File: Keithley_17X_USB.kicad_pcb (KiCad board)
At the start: 2 copper layers, 91.5 x 44 mm, 42 parts, among them J1 USB_B, J2 SIGNAL INPUT, J3 PROG, U1 TLP281-4, U2 TLP281-4, U3 MIC5504-3.3YM5, U4 MSP430FR2110, U5 FT230XS

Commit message: rearaned B1 B2 B4 and B8 connection to opto for better layout
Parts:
- moved U4 71.8 mm to (95.8, 56.2), turned to 90 degrees
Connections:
- J2 pad 3: /B8_IN -> /B1_IN
- J2 pad 5: /B4_IN -> /B2_IN
- J2 pad 7: /B2_IN -> /B4_IN
- J2 pad 9: /B1_IN -> /B8_IN
- U2 pad 1: /B1_IN -> /B8_IN
- U2 pad 10: /B8 -> /B1
- U2 pad 12: /B4 -> /B2
- U2 pad 14: /B2 -> /B4
- U2 pad 16: /B1 -> /B8
- U2 pad 3: /B2_IN -> /B4_IN
- U2 pad 5: /B4_IN -> /B2_IN
- U2 pad 7: /B8_IN -> /B1_IN
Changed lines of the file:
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@@
     (pad 2 thru_hole oval (at 2.54 0 180) (size 1.7 1.7) (drill 1) (layers *.Cu *.Mask))
     (pad 3 thru_hole oval (at 0 -2.54 180) (size 1.7 1.7) (drill 1) (layers *.Cu *.Mask)
-      (net 19 /B8_IN))
+      (net 23 /B1_IN))
     (pad 4 thru_hole oval (at 2.54 -2.54 180) (size 1.7 1.7) (drill 1) (layers *.Cu *.Mask))
     (pad 5 thru_hole oval (at 0 -5.08 180) (size 1.7 1.7) (drill 1) (layers *.Cu *.Mask)
-      (net 20 /B4_IN))
+      (net 22 /B2_IN))
     (pad 6 thru_hole oval (at 2.54 -5.08 180) (size 1.7 1.7) (drill 1) (layers *.Cu *.Mask)
       (net 21 /SIGN_IN))
     (pad 7 thru_hole oval (at 0 -7.62 180) (size 1.7 1.7) (drill 1) (layers *.Cu *.Mask)
-      (net 22 /B2_IN))
+      (net 20 /B4_IN))
     (pad 8 thru_hole oval (at 2.54 -7.62 180) (size 1.7 1.7) (drill 1) (layers *.Cu *.Mask))
     (pad 9 thru_hole oval (at 0 -10.16 180) (size 1.7 1.7) (drill 1) (layers *.Cu *.Mask)
-      (net 23 /B1_IN))
+      (net 19 /B8_IN))
     (pad 10 thru_hole oval (at 2.54 -10.16 180) (size 1.7 1.7) (drill 1) (layers *.Cu *.Mask))
     (pad 11 thru_hole oval (at 0 -12.7 180) (size 1.7 1.7) (drill 1) (layers *.Cu *.Mask)
@@
     (fp_line (start 0 5.26) (end 2.275 5.26) (layer F.SilkS) (width 0.12))
     (pad 16 smd roundrect (at 3.25 -4.445) (size 1.6 0.55) (layers F.Cu F.Paste F.Mask) (roundrect_rratio 0.25)
+      (net 49 /B8))
+    (pad 15 smd roundrect (at 3.25 -3.175) (size 1.6 0.55) (layers F.Cu F.Paste F.Mask) (roundrect_rratio 0.25)
+      (net 2 GND))
+    (pad 14 smd roundrect (at 3.25 -1.905) (size 1.6 0.55) (layers F.Cu F.Paste F.Mask) (roundrect_rratio 0.25)
+      (net 48 /B4))
+    (pad 13 smd roundrect (at 3.25 -0.635) (size 1.6 0.55) (layers F.Cu F.Paste F.Mask) (roundrect_rratio 0.25)
+      (net 2 GND))
+    (pad 12 smd roundrect (at 3.25 0.635) (size 1.6 0.55) (layers F.Cu F.Paste F.Mask) (roundrect_rratio 0.25)
+      (net 47 /B2))
+    (pad 11 smd roundrect (at 3.25 1.905) (size 1.6 0.55) (layers F.Cu F.Paste F.Mask) (roundrect_rratio 0.25)
+      (net 2 GND))
+    (pad 10 smd roundrect (at 3.25 3.175) (size 1.6 0.55) (layers F.Cu F.Paste F.Mask) (roundrect_rratio 0.25)
       (net 46 /B1))
-    (pad 15 smd roundrect (at 3.25 -3.175) (size 1.6 0.55) (layers F.Cu F.Paste F.Mask) (roundrect_rratio 0.25)
-      (net 2 GND))
-    (pad 14 smd roundrect (at 3.25 -1.905) (size 1.6 0.55) (layers F.Cu F.Paste F.Mask) (roundrect_rratio 0.25)
-      (net 47 /B2))
-    (pad 13 smd roundrect (at 3.25 -0.635) (size 1.6 0.55) (layers F.Cu F.Paste F.Mask) (roundrect_rratio 0.25)
-      (net 2 GND))
-    (pad 12 smd roundrect (at 3.25 0.635) (size 1.6 0.55) (layers F.Cu F.Paste F.Mask) (roundrect_rratio 0.25)
-      (net 48 /B4))
-    (pad 11 smd roundrect (at 3.25 1.905) (size 1.6 0.55) (layers F.Cu F.Paste F.Mask) (roundrect_rratio 0.25)
-      (net 2 GND))
-    (pad 10 smd roundrect (at 3.25 3.175) (size 1.6 0.55) (layers F.Cu F.Paste F.Mask) (roundrect_rratio 0.25)
-      (net 49 /B8))
     (pad 9 smd roundrect (at 3.25 4.445) (size 1.6 0.55) (layers F.Cu F.Paste F.Mask) (roundrect_rratio 0.25)
       (net 2 GND))
@@
       (net 41 "Net-(RN2-Pad5)"))
     (pad 7 smd roundrect (at -3.25 3.175) (size 1.6 0.55) (layers F.Cu F.Paste F.Mask) (roundrect_rratio 0.25)
-      (net 19 /B8_IN))
+      (net 23 /B1_IN))
     (pad 6 smd roundrect (at -3.25 1.905) (size 1.6 0.55) (layers F.Cu F.Paste F.Mask) (roundrect_rratio 0.25)
       (net 40 "Net-(RN2-Pad6)"))
     (pad 5 smd roundrect (at -3.25 0.635) (size 1.6 0.55) (layers F.Cu F.Paste F.Mask) (roundrect_rratio 0.25)
-      (net 20 /B4_IN))
+      (net 22 /B2_IN))
     (pad 4 smd roundrect (at -3.25 -0.635) (size 1.6 0.55) (layers F.Cu F.Paste F.Mask) (roundrect_rratio 0.25)
       (net 39 "Net-(RN2-Pad7)"))
     (pad 3 smd roundrect (at -3.25 -1.905) (size 1.6 0.55) (layers F.Cu F.Paste F.Mask) (roundrect_rratio 0.25)
-      (net 22 /B2_IN))
+      (net 20 /B4_IN))
     (pad 2 smd roundrect (at -3.25 -3.175) (size 1.6 0.55) (layers F.Cu F.Paste F.Mask) (roundrect_rratio 0.25)
       (net 38 "Net-(RN2-Pad8)"))
     (pad 1 smd roundrect (at -3.25 -4.445) (size 1.6 0.55) (layers F.Cu F.Paste F.Mask) (roundrect_rratio 0.25)
-      (net 23 /B1_IN))
+      (net 19 /B8_IN))
     (model ${KIPRJMOD}/3d_models/SOIC-16_3.9x9.9mm_p1.27mm.wrl
       (at (xyz 0 0 0))
@@
   )
   (module Package_SO:TSSOP-16_4.4x5mm_P0.65mm (layer F.Cu)
-    (at 46 108)
+    (at 95.75 56.25 90)
     (descr "16-Lead Plastic Thin Shrink Small Outline (ST)-4.4 mm Body [TSSOP] (see Microchip Packaging Specification 00000049BS.pdf)")
     (tags "SSOP 0.65")
     (attr smd)
-    (fp_text reference U4 (at 0 -3.55) (layer F.SilkS)
-      (effects (font (size 1 1) (thickness 0.15)))
-    )
-    (fp_text value MSP430FR2110 (at 0 3.55) (layer F.Fab)
+    (fp_text reference U4 (at 0 -3.55 90) (layer F.SilkS)
+      (effects (font (size 1 1) (thickness 0.15)))
+    )
+    (fp_text value MSP430FR2110 (at 0 3.55 90) (layer F.Fab)
       (effects (font (size 1 1) (thickness 0.15)))
     )
@@
     (fp_line (start -2.2 2.725) (end 2.2 2.725) (layer F.SilkS) (width 0.15))
     (fp_line (start -3.775 -2.8) (end 2.2 -2.8) (layer F.SilkS) (width 0.15))
-    (fp_text user %R (at 0 0) (layer F.Fab)
+    (fp_text user %R (at 0 0 90) (layer F.Fab)
       (effects (font (size 0.8 0.8) (thickness 0.15)))
     )
-    (pad 1 smd rect (at -2.95 -2.275) (size 1.5 0.45) (layers F.Cu F.Paste F.Mask)
+    (pad 1 smd rect (at -2.95 -2.275 90) (size 1.5 0.45) (layers F.Cu F.Paste F.Mask)
       (net 47 /B2))
-    (pad 2 smd rect (at -2.95 -1.625) (size 1.5 0.45) (layers F.Cu F.Paste F.Mask)
+    (pad 2 smd rect (at -2.95 -1.625 90) (size 1.5 0.45) (layers F.Cu F.Paste F.Mask)
       (net 46 /B1))
-    (pad 3 smd rect (at -2.95 -0.975) (size 1.5 0.45) (layers F.Cu F.Paste F.Mask)
+    (pad 3 smd rect (at -2.95 -0.975 90) (size 1.5 0.45) (layers F.Cu F.Paste F.Mask)
       (net 28 /SBWTCK))
-    (pad 4 smd rect (at -2.95 -0.325) (size 1.5 0.45) (layers F.Cu F.Paste F.Mask)
+    (pad 4 smd rect (at -2.95 -0.325 90) (size 1.5 0.45) (layers F.Cu F.Paste F.Mask)
       (net 27 /SBWTDIO))
-    (pad 5 smd rect (at -2.95 0.325) (size 1.5 0.45) (layers F.Cu F.Paste F.Mask)
+    (pad 5 smd rect (at -2.95 0.325 90) (size 1.5 0.45) (layers F.Cu F.Paste F.Mask)
       (net 3 +3V3))
-    (pad 6 smd rect (at -2.95 0.975) (size 1.5 0.45) (layers F.Cu F.Paste F.Mask)
-      (net 2 GND))
-    (pad 7 smd rect (at -2.95 1.625) (size 1.5 0.45) (layers F.Cu F.Paste F.Mask)
+    (pad 6 smd rect (at -2.95 0.975 90) (size 1.5 0.45) (layers F.Cu F.Paste F.Mask)
+      (net 2 GND))
+    (pad 7 smd rect (at -2.95 1.625 90) (size 1.5 0.45) (layers F.Cu F.Paste F.Mask)
       (net 42 /OVERRANGE))
-    (pad 8 smd rect (at -2.95 2.275) (size 1.5 0.45) (layers F.Cu F.Paste F.Mask)
+    (pad 8 smd rect (at -2.95 2.275 90) (size 1.5 0.45) (layers F.Cu F.Paste F.Mask)
       (net 43 /SIGN))
-    (pad 9 smd rect (at 2.95 2.275) (size 1.5 0.45) (layers F.Cu F.Paste F.Mask)
+    (pad 9 smd rect (at 2.95 2.275 90) (size 1.5 0.45) (layers F.Cu F.Paste F.Mask)
       (net 44 /D5))
-    (pad 10 smd rect (at 2.95 1.625) (size 1.5 0.45) (layers F.Cu F.Paste F.Mask)
+    (pad 10 smd rect (at 2.95 1.625 90) (size 1.5 0.45) (layers F.Cu F.Paste F.Mask)
       (net 45 /CLK))
-    (pad 11 smd rect (at 2.95 0.975) (size 1.5 0.45) (layers F.Cu F.Paste F.Mask)
+    (pad 11 smd rect (at 2.95 0.975 90) (size 1.5 0.45) (layers F.Cu F.Paste F.Mask)
       (net 50 /RXD))
-    (pad 12 smd rect (at 2.95 0.325) (size 1.5 0.45) (layers F.Cu F.Paste F.Mask)
+    (pad 12 smd rect (at 2.95 0.325 90) (size 1.5 0.45) (layers F.Cu F.Paste F.Mask)
       (net 51 /TXD))
-    (pad 13 smd rect (at 2.95 -0.325) (size 1.5 0.45) (layers F.Cu F.Paste F.Mask)
+    (pad 13 smd rect (at 2.95 -0.325 90) (size 1.5 0.45) (layers F.Cu F.Paste F.Mask)
       (net 30 /RATE))
-    (pad 14 smd rect (at 2.95 -0.975) (size 1.5 0.45) (layers F.Cu F.Paste F.Mask)
+    (pad 14 smd rect (at 2.95 -0.975 90) (size 1.5 0.45) (layers F.Cu F.Paste F.Mask)
       (net 16 /READ))
-    (pad 15 smd rect (at 2.95 -1.625) (size 1.5 0.45) (layers F.Cu F.Paste F.Mask)
+    (pad 15 smd rect (at 2.95 -1.625 90) (size 1.5 0.45) (layers F.Cu F.Paste F.Mask)
       (net 49 /B8))
-    (pad 16 smd rect (at 2.95 -2.275) (size 1.5 0.45) (layers F.Cu F.Paste F.Mask)
+    (pad 16 smd rect (at 2.95 -2.275 90) (size 1.5 0.45) (layers F.Cu F.Paste F.Mask)
       (net 48 /B4))
     (model ${KISYS3DMOD}/Package_SO.3dshapes/TSSOP-16_4.4x5mm_P0.65mm.wrl

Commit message: update 3d model to shrouded header
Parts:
- moved U5 16.5 mm to (116.5, 67.0)
- moved U2 9.72 mm to (73.0, 63.8)
- moved U1 6.32 mm to (73.0, 79.0)
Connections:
- J2 pad 3: /B1_IN -> /B8_IN
- J2 pad 5: /B2_IN -> /B4_IN
- J2 pad 7: /B4_IN -> /B2_IN
- J2 pad 9: /B8_IN -> /B1_IN
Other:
- board size 91.5 x 44 mm -> 87 x 44 mm
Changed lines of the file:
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@@
     (pad 2 thru_hole oval (at 2.54 0 180) (size 1.7 1.7) (drill 1) (layers *.Cu *.Mask))
     (pad 3 thru_hole oval (at 0 -2.54 180) (size 1.7 1.7) (drill 1) (layers *.Cu *.Mask)
-      (net 23 /B1_IN))
+      (net 19 /B8_IN))
     (pad 4 thru_hole oval (at 2.54 -2.54 180) (size 1.7 1.7) (drill 1) (layers *.Cu *.Mask))
     (pad 5 thru_hole oval (at 0 -5.08 180) (size 1.7 1.7) (drill 1) (layers *.Cu *.Mask)
-      (net 22 /B2_IN))
+      (net 20 /B4_IN))
     (pad 6 thru_hole oval (at 2.54 -5.08 180) (size 1.7 1.7) (drill 1) (layers *.Cu *.Mask)
       (net 21 /SIGN_IN))
     (pad 7 thru_hole oval (at 0 -7.62 180) (size 1.7 1.7) (drill 1) (layers *.Cu *.Mask)
-      (net 20 /B4_IN))
+      (net 22 /B2_IN))
     (pad 8 thru_hole oval (at 2.54 -7.62 180) (size 1.7 1.7) (drill 1) (layers *.Cu *.Mask))
     (pad 9 thru_hole oval (at 0 -10.16 180) (size 1.7 1.7) (drill 1) (layers *.Cu *.Mask)
-      (net 19 /B8_IN))
+      (net 23 /B1_IN))
     (pad 10 thru_hole oval (at 2.54 -10.16 180) (size 1.7 1.7) (drill 1) (layers *.Cu *.Mask))
     (pad 11 thru_hole oval (at 0 -12.7 180) (size 1.7 1.7) (drill 1) (layers *.Cu *.Mask)
@@
       (net 26 /D5_IN))
     (pad 14 thru_hole oval (at 2.54 -15.24 180) (size 1.7 1.7) (drill 1) (layers *.Cu *.Mask))
-    (model ${KISYS3DMOD}/Connector_PinHeader_2.54mm.3dshapes/PinHeader_2x07_P2.54mm_Horizontal.wrl
+    (model ${KIPRJMOD}/3d_models/Header_14pos_2rows_RightAngle_Shrouded.wrl
       (at (xyz 0 0 0))
       (scale (xyz 1 1 1))
@@
   )
   (module Package_SO:SOIC-16_4.55x10.3mm_P1.27mm (layer F.Cu)
-    (at 79 77)
+    (at 73 79)
     (descr "SOIC, 16 Pin (https://toshiba.semicon-storage.com/info/docget.jsp?did=12858&prodName=TLP291-4), generated with kicad-footprint-generator ipc_gullwing_generator.py")
     (tags "SOIC SO")
@@
   )
   (module Package_SO:SOIC-16_4.55x10.3mm_P1.27mm (layer F.Cu)
-    (at 80 57)
+    (at 73 63.75)
     (descr "SOIC, 16 Pin (https://toshiba.semicon-storage.com/info/docget.jsp?did=12858&prodName=TLP291-4), generated with kicad-footprint-generator ipc_gullwing_generator.py")
     (tags "SOIC SO")
@@
   )
   (module Package_SO:SSOP-16_3.9x4.9mm_P0.635mm (layer F.Cu)
-    (at 100 66 90)
+    (at 116.5 67 90)
     (descr "SSOP16: plastic shrink small outline package; 16 leads; body width 3.9 mm; lead pitch 0.635; (see NXP SSOP-TSSOP-VSO-REFLOW.pdf and sot519-1_po.pdf)")
     (tags "SSOP 0.635")
@@
   (gr_line (start 145 86.5) (end 146.5 86) (layer Dwgs.User) (width 0.1))
   (gr_line (start 145 85.5) (end 146.5 85) (layer Dwgs.User) (width 0.1))
-  (gr_line (start 141.5 93.25) (end 50 93.25) (layer Edge.Cuts) (width 0.15))
-  (gr_line (start 141.5 49.25) (end 50 49.25) (layer Edge.Cuts) (width 0.15))
+  (gr_line (start 141.5 93.25) (end 54.5 93.25) (layer Edge.Cuts) (width 0.15))
+  (gr_line (start 141.5 49.25) (end 54.5 49.25) (layer Edge.Cuts) (width 0.15))
   (gr_line (start 141.5 93.25) (end 141.5 49.25) (layer Edge.Cuts) (width 0.15))
   (gr_text CL (at 169.25 71.25) (layer Dwgs.User)
@@
     (effects (font (size 2 2) (thickness 0.3)) (justify left))
   )
-  (gr_line (start 50 49.25) (end 50 93.25) (layer Edge.Cuts) (width 0.15))
+  (gr_line (start 54.5 49.25) (end 54.5 93.25) (layer Edge.Cuts) (width 0.15))
 )

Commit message: Update Keithley_17X_USB.kicad_pcb
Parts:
- moved H2 45.6 mm to (117.5, 101.5)
- moved H1 41.3 mm to (114.5, 37.6)
- moved U4 20.7 mm to (81.5, 71.2)
- moved D2 1.44 mm to (127.2, 75.0)
- moved RN2 1.12 mm to (63.0, 56.5)
- moved D1 1.10 mm to (128.5, 69.5)
- moved RN1 1.03 mm to (63.0, 86.2)
- moved D3 0.94 mm to (124.7, 66.0)
- moved R1 0.94 mm to (124.7, 73.5)
- moved R2 0.94 mm to (124.7, 76.5)
- moved TH1 0.94 mm to (124.7, 70.0)
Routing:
- net /SIGN_IN: track 0.00 -> 21.5 mm
- net /CLK_IN: track 0.00 -> 19.8 mm
- net /OVERRANGE_IN: track 0.00 -> 16.6 mm
- net Net-(RN2-Pad5): track 0.00 -> 14.7 mm, vias 0 -> 2
- net Net-(RN2-Pad6): track 0.00 -> 13.8 mm, vias 0 -> 2
- net Net-(RN1-Pad8): track 0.00 -> 12.8 mm, vias 0 -> 2
- net Net-(RN2-Pad7): track 0.00 -> 12.4 mm, vias 0 -> 2
- net /B4_IN: track 0.00 -> 11.9 mm
- net Net-(RN1-Pad7): track 0.00 -> 11.9 mm, vias 0 -> 2
- net /B2_IN: track 0.00 -> 11.8 mm
- net /B1_IN: track 0.00 -> 11.5 mm
- net Net-(RN2-Pad8): track 0.00 -> 11.1 mm, vias 0 -> 2
- net Net-(RN1-Pad6): track 0.00 -> 11.1 mm, vias 0 -> 2
- net /B8_IN: track 0.00 -> 10.8 mm
- net /D+: track 0.00 -> 10.2 mm
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- added copper zone on B.Cu, net GNDA
- added copper zone on F.Cu, net GNDA
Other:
- outline, holes or cut-outs redrawn
- net class USB_data added: clearance 0.2, trace_width 0.25, via_dia 0.8, via_drill 0.4
- board text added: "Isolation Line Do Not Cross"
- board text added: "To Keithley J1008"

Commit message: Update Keithley_17X_USB.kicad_pcb
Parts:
- moved U3 121.2 mm to (105.3, 63.5), turned to 90 degrees
- moved D4 119.5 mm to (112.5, 53.0), turned to 270 degrees
- moved R4 117.0 mm to (109.2, 56.8), turned to 90 degrees
- moved C1 105.9 mm to (108.4, 63.5), turned to 90 degrees
- moved R3 104.6 mm to (112.5, 56.8), turned to 90 degrees
- moved C7 94.1 mm to (118.1, 70.3)
- moved D5 92.1 mm to (109.2, 53.0), turned to 270 degrees
- moved R5 91.1 mm to (108.8, 79.5)
- moved C4 90.3 mm to (88.1, 73.4)
- moved C5 89.9 mm to (114.9, 68.3), turned to 180 degrees
- moved C6 86.5 mm to (114.9, 70.3), turned to 180 degrees
- moved C2 83.4 mm to (102.2, 63.5), turned to 270 degrees
- moved C3 77.6 mm to (87.0, 77.2)
- moved D7 73.9 mm to (110.0, 89.5), turned to 270 degrees
- moved D6 69.5 mm to (106.5, 89.5), turned to 270 degrees
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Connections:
- net Net-(R1-Pad1) renamed /USBD_N
- net Net-(R2-Pad1) renamed /USBD_P
- C7 pad 1: Net-(C7-Pad1) -> /VCCIO
- H5 pad 1: (no net) -> GND
- H6 pad 1: (no net) -> GND
- J1 pad 5: Net-(J1-Pad5) -> GND
- R5 pad 1: +5V -> /VCCIO
- R6 pad 1: +5V -> /VCCIO
- U5 pad 10: Net-(C7-Pad1) -> /VCCIO
- U5 pad 11: Net-(C7-Pad1) -> /VCCIO
- U5 pad 3: Net-(C7-Pad1) -> /VCCIO
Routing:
- net +5V: track 0.00 -> 14.2 mm
- net /VCCIO: track 0.00 -> 8.78 mm
- net GND: track 1.90 -> 8.10 mm, vias 2 -> 7
- net Net-(D3-Pad2): track 0.00 -> 5.22 mm
- net /USBD_P: track 0.00 -> 4.85 mm
- net /USBD_N: track 0.00 -> 4.85 mm
- net /D+: track 10.2 -> 11.0 mm
- added copper zone on B.Cu, net GND
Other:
- board size 87 x 44 mm -> 85.5 x 44 mm
- net class Power added: clearance 0.2, trace_width 0.8, via_dia 0.8, via_drill 0.4

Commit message: Update Keithley_17X_USB.kicad_pcb
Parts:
- moved J3 57.0 mm to (90.5, 90.1), turned to 90 degrees
- moved H2 38.7 mm to (80.6, 90.1)
- moved H1 37.0 mm to (80.6, 52.4)
- moved D6 19.2 mm to (125.2, 85.2), turned to 180 degrees
- moved D5 18.6 mm to (125.2, 62.6), turned to 180 degrees
- moved D4 17.5 mm to (125.2, 65.2), turned to 180 degrees
- moved U4 16.7 mm to (87.3, 71.2)
- moved D7 16.6 mm to (125.2, 82.7), turned to 180 degrees
- moved R4 13.6 mm to (121.5, 62.6), turned to 0 degrees
- moved R5 13.2 mm to (120.8, 85.2)
- moved C2 12.5 mm to (114.1, 67.3), turned to 0 degrees
- moved R3 12.3 mm to (121.5, 65.2), turned to 0 degrees
- moved R6 12.3 mm to (120.8, 82.7)
- moved C3 9.38 mm to (79.3, 71.9), turned to 270 degrees
- moved U3 8.83 mm to (114.1, 64.2), turned to 180 degrees
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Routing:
- net GND: track 8.10 -> 25.9 mm, vias 7 -> 19
- net +5V: track 14.2 -> 27.4 mm
- net Net-(D1-Pad1): track 5.90 -> 0.00 mm
- net Net-(D3-Pad2): track 5.22 -> 0.00 mm
- net /USBD_P: track 4.85 -> 7.84 mm
- net /USBD_N: track 4.85 -> 7.84 mm
- net /VCCIO: track 8.78 -> 11.8 mm
- net +3V3: track 0.00 -> 2.28 mm
- net Net-(D5-Pad2): track 0.00 -> 1.98 mm
- net Net-(D4-Pad2): track 0.00 -> 1.98 mm
- net /RXLED: track 0.00 -> 1.56 mm, vias 0 -> 1
- added copper zone on F.Cu, net Net-(D1-Pad1)
- added copper zone on F.Cu, net Net-(D3-Pad2)

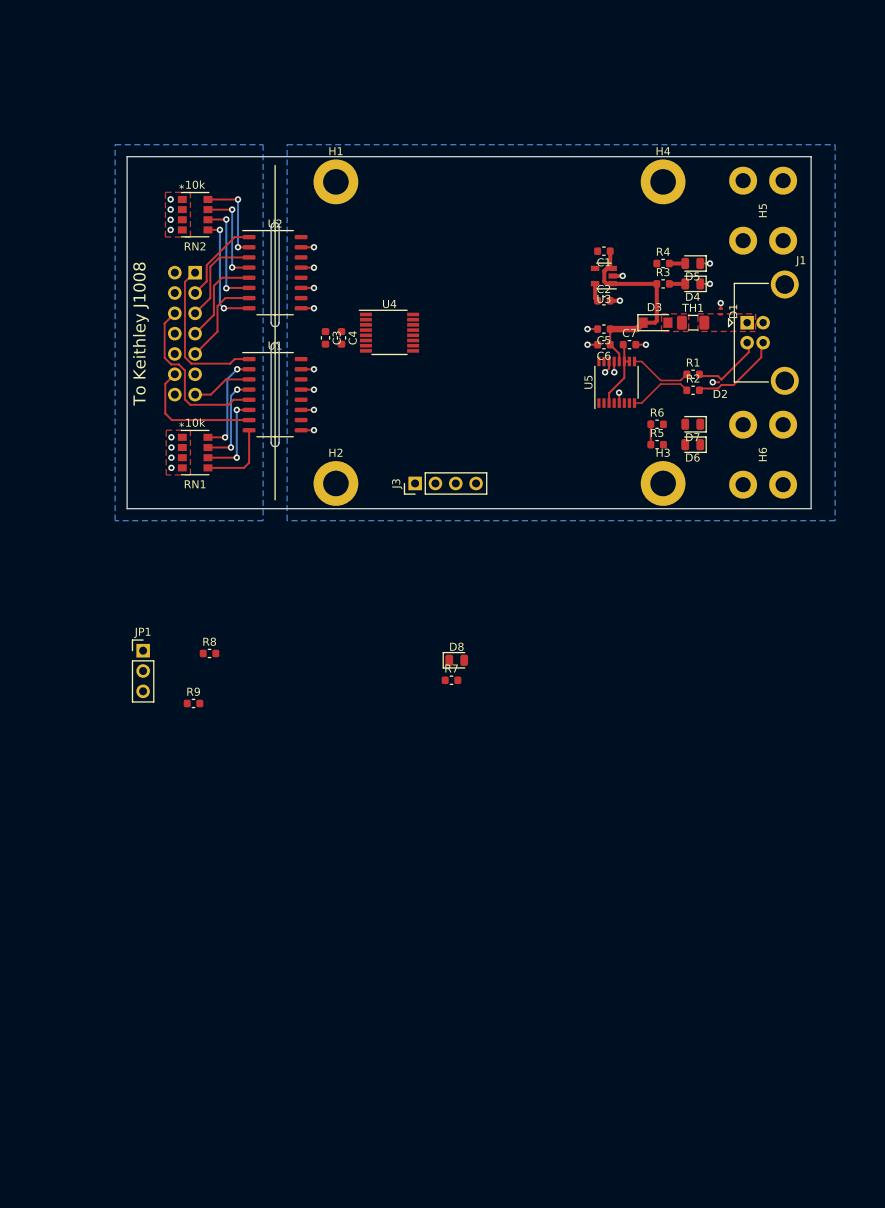
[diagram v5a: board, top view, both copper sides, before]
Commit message: shrink length by 15mm
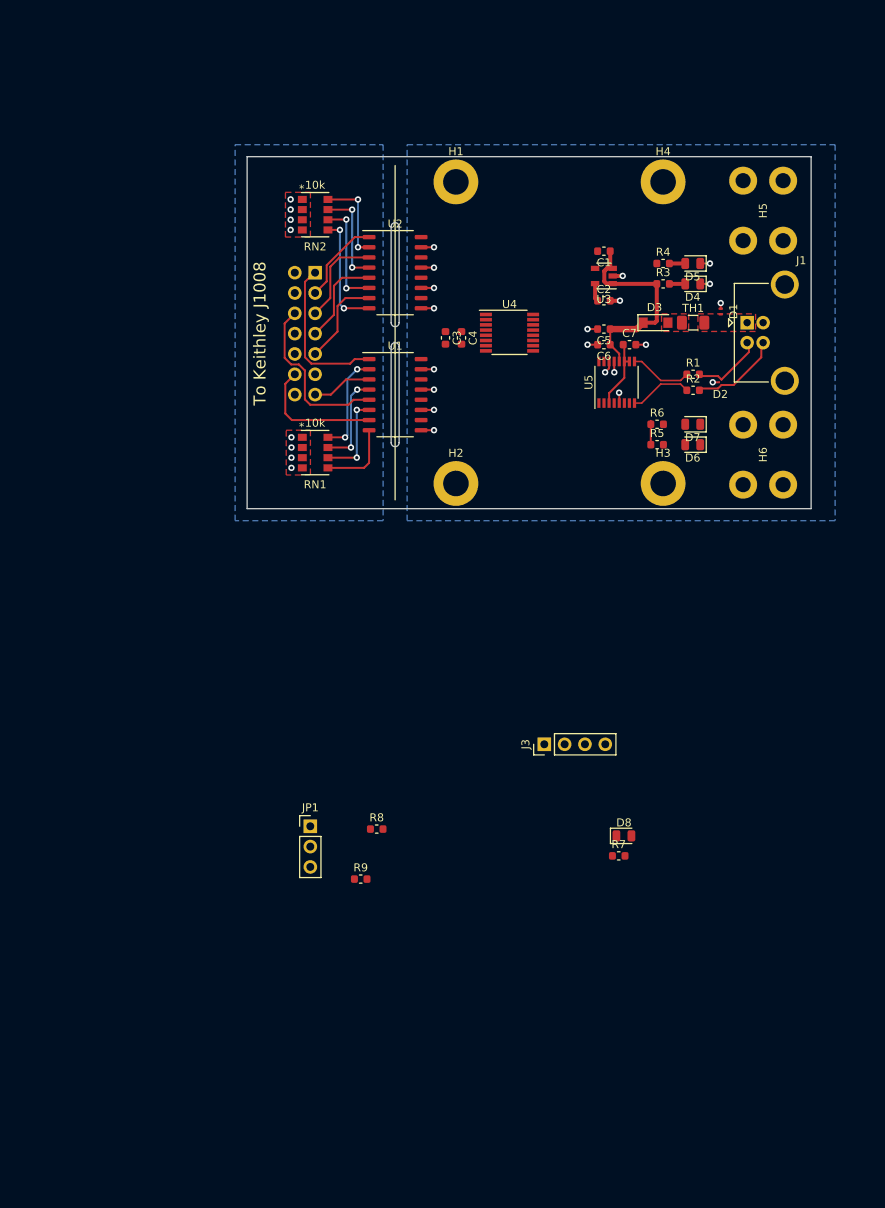
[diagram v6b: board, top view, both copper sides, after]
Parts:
- moved J3 36.4 mm to (106.7, 122.7)
- moved R8 30.3 mm to (85.7, 133.3)
- moved R9 30.3 mm to (83.7, 139.6)
- moved R7 30.3 mm to (116.0, 136.7)
- moved D8 30.3 mm to (116.6, 134.2)
- moved JP1 30.3 mm to (77.4, 132.9)
- moved C3 15.0 mm to (94.3, 71.9)
- moved C4 15.0 mm to (96.3, 71.9)
- moved H1 15.0 mm to (95.6, 52.4)
- moved H2 15.0 mm to (95.6, 90.1)
- moved J2 15.0 mm to (78.0, 63.8)
- moved RN1 15.0 mm to (78.0, 86.2)
- moved RN2 15.0 mm to (78.0, 56.5)
- moved U1 15.0 mm to (88.0, 79.0)
- moved U2 15.0 mm to (88.0, 63.8)
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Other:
- board size 85.5 x 44 mm -> 70.5 x 44 mm
